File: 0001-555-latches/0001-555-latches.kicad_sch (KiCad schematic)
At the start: 27 parts, among them J1 DC_IN, J2 ASTBL_OUT, J3 MSTBL_OUT, J4 BSTBL_OUT, SW1 SW_Push, SW2 SW_Push, SW3 SW_Push, U1 NE555P, U2 NE555P, U3 NE555P

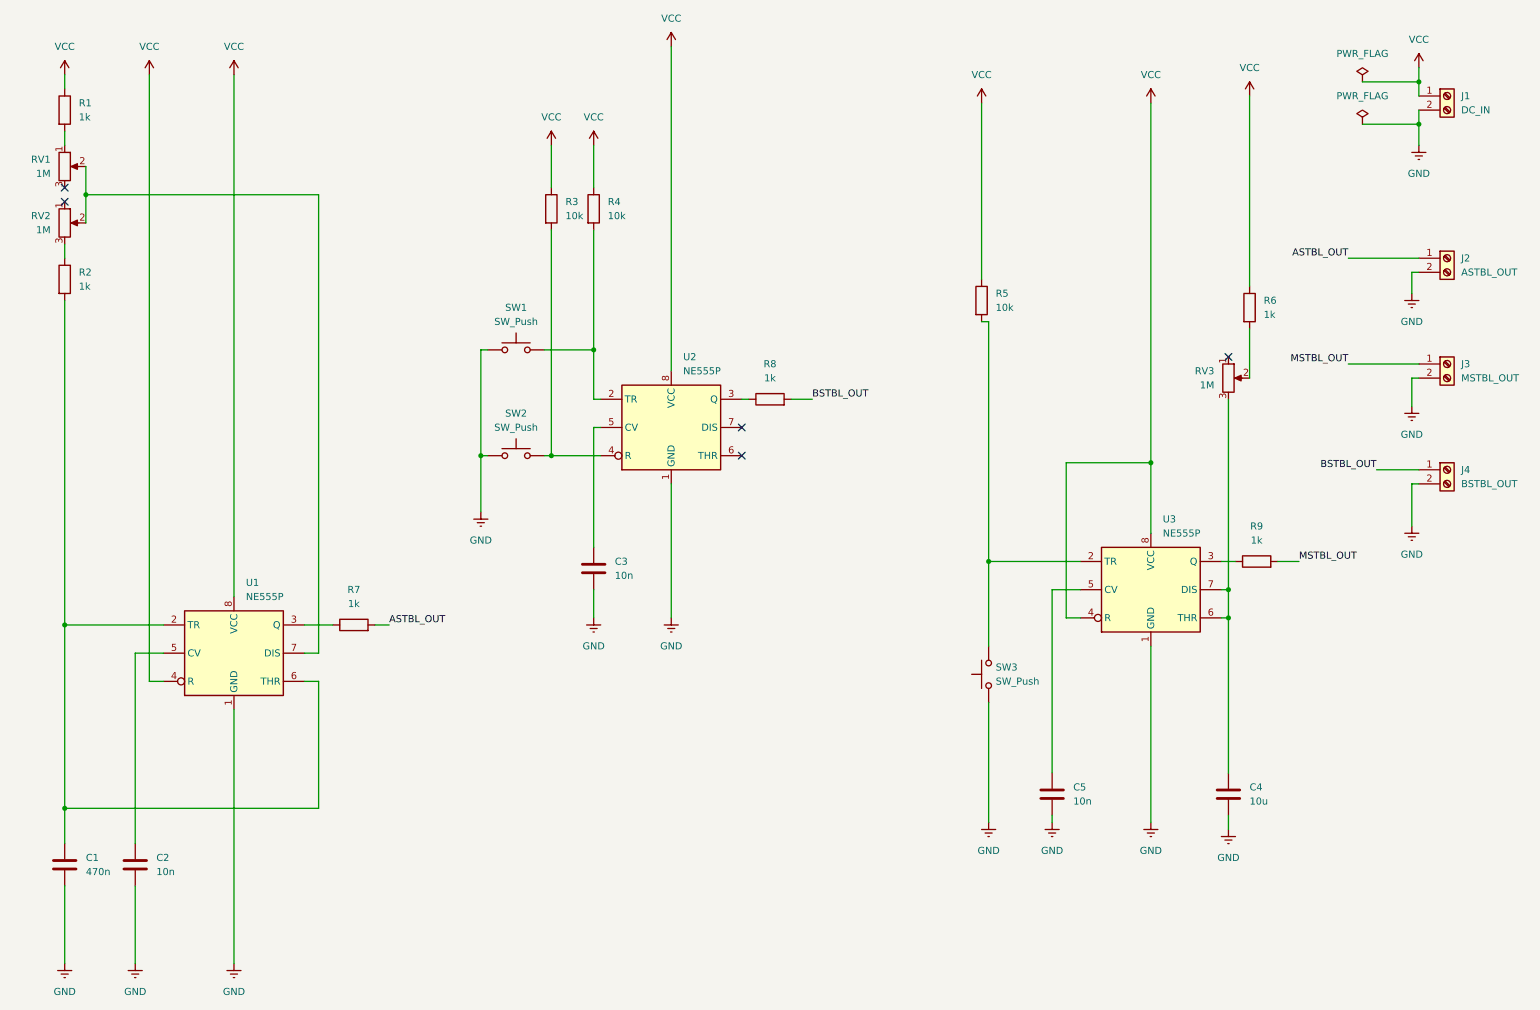
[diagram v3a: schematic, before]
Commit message: Update values and symbols of monostable capacitor
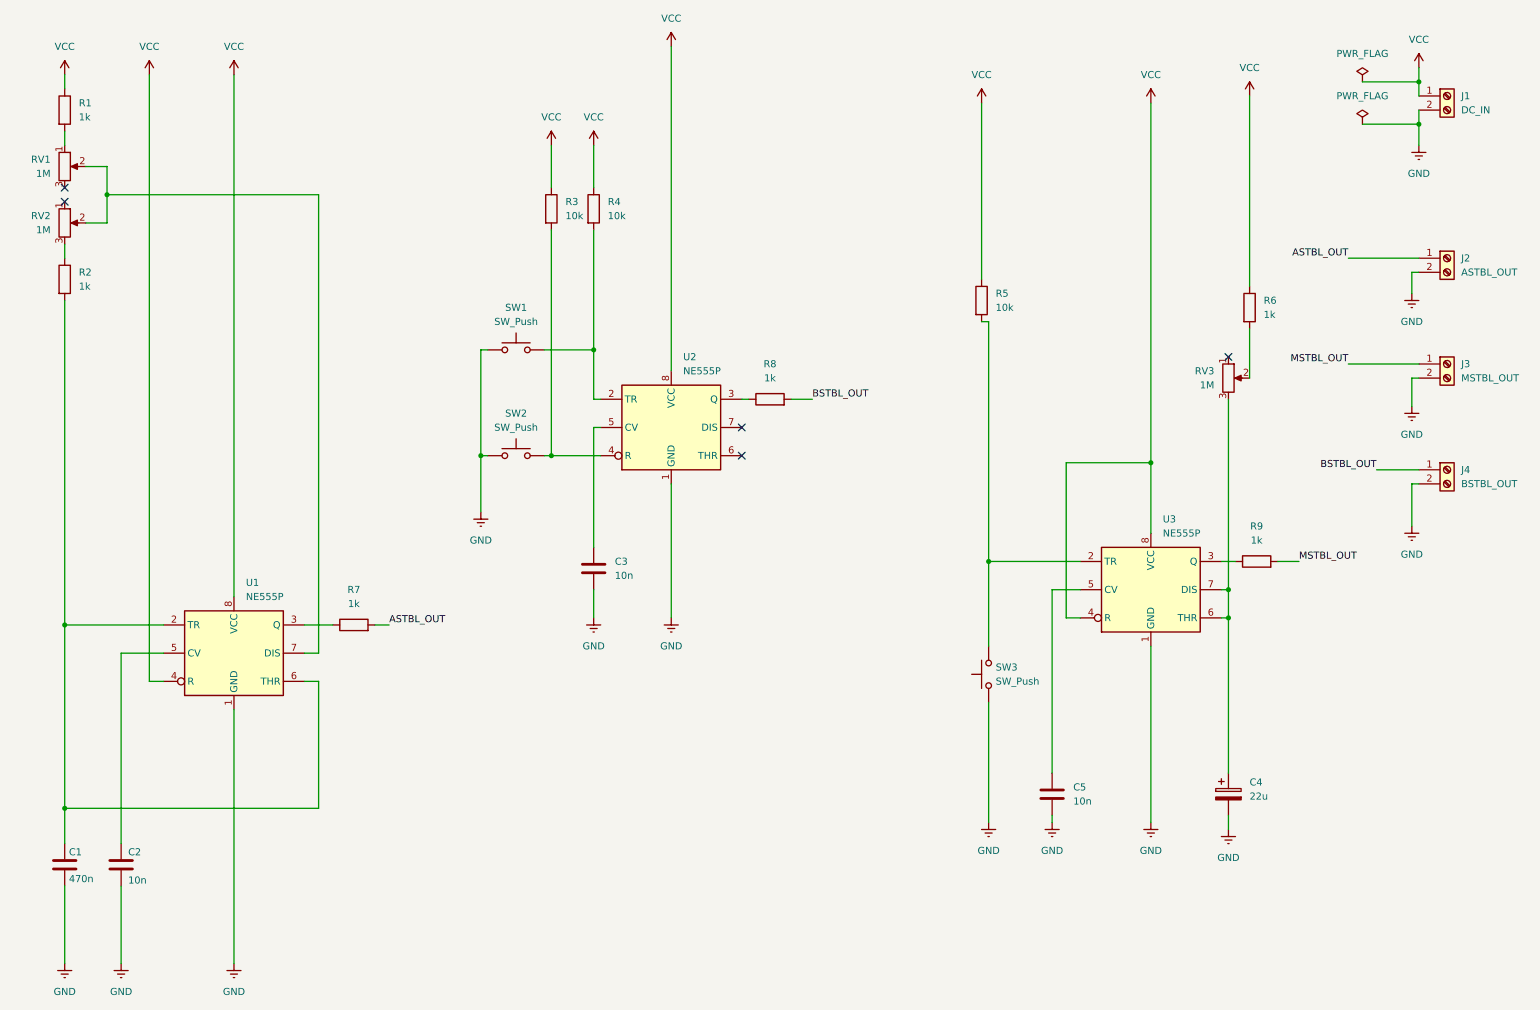
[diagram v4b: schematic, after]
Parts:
- removed C4: 10u, symbol Device:C
- added C4: 22u, symbol Device:C_Polarized
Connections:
- net GND: now also C4.2
- net at RV3.3, U3.6 (THR), U3.7 (DIS): now also C4.1
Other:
- moved on the sheet: C2
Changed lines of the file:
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@@
 	)
 	(junction
-		(at 24.13 46.99)
+		(at 27.94 46.99)
 		(diameter 0)
 		(color 0 0 0 0)
@@
 	(wire
 		(pts
-			(xy 24.13 41.91) (xy 24.13 46.99)
+			(xy 27.94 41.91) (xy 27.94 46.99)
 		)
 		(stroke
@@
 	(wire
 		(pts
-			(xy 33.02 163.83) (xy 33.02 129.54)
+			(xy 30.48 163.83) (xy 30.48 129.54)
 		)
 		(stroke
@@
 	(wire
 		(pts
-			(xy 33.02 171.45) (xy 33.02 185.42)
+			(xy 30.48 171.45) (xy 30.48 185.42)
 		)
 		(stroke
@@
 	(wire
 		(pts
+			(xy 27.94 52.07) (xy 24.13 52.07)
+		)
+		(stroke
+			(width 0)
+			(type default)
+		)
+	)
+	(wire
+		(pts
 			(xy 264.16 38.1) (xy 264.16 34.29)
 		)
@@
 	(wire
 		(pts
-			(xy 24.13 46.99) (xy 66.04 46.99)
+			(xy 27.94 46.99) (xy 66.04 46.99)
 		)
 		(stroke
@@
 	(wire
 		(pts
-			(xy 24.13 46.99) (xy 24.13 52.07)
+			(xy 27.94 46.99) (xy 27.94 52.07)
 		)
 		(stroke
@@
 	(wire
 		(pts
+			(xy 27.94 41.91) (xy 24.13 41.91)
+		)
+		(stroke
+			(width 0)
+			(type default)
+		)
+	)
+	(wire
+		(pts
 			(xy 66.04 134.62) (xy 63.5 134.62)
 		)
@@
 	(wire
 		(pts
-			(xy 33.02 129.54) (xy 38.1 129.54)
+			(xy 30.48 129.54) (xy 38.1 129.54)
 		)
 		(stroke
@@
 	(symbol
 		(lib_id "power:GNDREF")
-		(at 33.02 185.42 0)
+		(at 30.48 185.42 0)
 		(unit 1)
 		(exclude_from_sim no)
@@
 		(fields_autoplaced yes)
 		(property "Reference" "#PWR03"
-			(at 33.02 191.77 0)
+			(at 30.48 191.77 0)
 			(effects
 				(font
@@
 		)
 		(property "Value" "GND"
-			(at 33.02 190.5 0)
+			(at 30.48 190.5 0)
 			(effects
 				(font
@@
 		)
 		(property "Footprint" ""
-			(at 33.02 185.42 0)
+			(at 30.48 185.42 0)
 			(effects
 				(font
@@
 		)
 		(property "Datasheet" ""
-			(at 33.02 185.42 0)
+			(at 30.48 185.42 0)
 			(effects
 				(font
@@
 		)
 		(property "Description" "Power symbol creates a global label with name \"GNDREF\" , reference supply ground"
-			(at 33.02 185.42 0)
+			(at 30.48 185.42 0)
 			(effects
 				(font
@@
 	(symbol
 		(lib_id "Device:C")
-		(at 33.02 167.64 0)
+		(at 30.48 167.64 0)
 		(unit 1)
 		(exclude_from_sim no)
@@
 		(on_board yes)
 		(dnp no)
-		(fields_autoplaced yes)
 		(property "Reference" "C2"
-			(at 36.83 166.3699 0)
+			(at 31.75 165.354 0)
 			(effects
 				(font
@@
 		)
 		(property "Value" "10n"
-			(at 36.83 168.9099 0)
+			(at 31.75 170.434 0)
 			(effects
 				(font
@@
 		)
 		(property "Footprint" ""
-			(at 33.9852 171.45 0)
+			(at 31.4452 171.45 0)
 			(effects
 				(font
@@
 		)
 		(property "Datasheet" "~"
-			(at 33.02 167.64 0)
+			(at 30.48 167.64 0)
 			(effects
 				(font
@@
 		)
 		(property "Description" "Unpolarized capacitor"
-			(at 33.02 167.64 0)
+			(at 30.48 167.64 0)
 			(effects
 				(font
@@
 		(on_board yes)
 		(dnp no)
-		(fields_autoplaced yes)
 		(property "Reference" "C1"
-			(at 24.13 166.3699 0)
+			(at 21.082 165.354 0)
 			(effects
 				(font
@@
 		)
 		(property "Value" "470n"
-			(at 24.13 168.9099 0)
+			(at 21.082 170.18 0)
 			(effects
 				(font
@@
 	)
 	(symbol
+		(lib_id "Device:C_Polarized")
+		(at 229.87 154.94 0)
+		(unit 1)
+		(exclude_from_sim no)
+		(in_bom yes)
+		(on_board yes)
+		(dnp no)
+		(fields_autoplaced yes)
+		(property "Reference" "C4"
+			(at 233.68 152.7809 0)
+			(effects
+				(font
+					(size 1.27 1.27)
+				)
+				(justify left)
+			)
+		)
+		(property "Value" "22u"
+			(at 233.68 155.3209 0)
+			(effects
+				(font
+					(size 1.27 1.27)
+				)
+				(justify left)
+			)
+		)
+		(property "Footprint" ""
+			(at 230.8352 158.75 0)
+			(effects
+				(font
+					(size 1.27 1.27)
+				)
+				(hide yes)
+			)
+		)
+		(property "Datasheet" "~"
+			(at 229.87 154.94 0)
+			(effects
+				(font
+					(size 1.27 1.27)
+				)
+				(hide yes)
+			)
+		)
+		(property "Description" "Polarized capacitor"
+			(at 229.87 154.94 0)
+			(effects
+				(font
+					(size 1.27 1.27)
+				)
+				(hide yes)
+			)
+		)
+		(pin "1"
+		)
+		(pin "2"
+		)
+		(instances
+			(project ""
+				(path "/11cec59d-a989-4950-8b21-3f1fb45ca1cc"
+					(reference "C4")
+					(unit 1)
+				)
+			)
+		)
+	)
+	(symbol
 		(lib_id "Connector:Screw_Terminal_01x02")
 		(at 269.24 29.21 0)
@@
 					(unit 1)
 				)
-			)
-		)
-	)
-	(symbol
-		(lib_id "Device:C")
-		(at 229.87 154.94 0)
-		(unit 1)
-		(exclude_from_sim no)
-		(in_bom yes)
-		(on_board yes)
-		(dnp no)
-		(fields_autoplaced yes)
-		(property "Reference" "C4"
-			(at 233.68 153.6699 0)
-			(effects
-				(font
-					(size 1.27 1.27)
-				)
-				(justify left)
-			)
-		)
-		(property "Value" "10u"
-			(at 233.68 156.2099 0)
-			(effects
-				(font
-					(size 1.27 1.27)
-				)
-				(justify left)
-			)
-		)
-		(property "Footprint" ""
-			(at 230.8352 158.75 0)
-			(effects
-				(font
-					(size 1.27 1.27)
-				)
-				(hide yes)
-			)
-		)
-		(property "Datasheet" "~"
-			(at 229.87 154.94 0)
-			(effects
-				(font
-					(size 1.27 1.27)
-				)
-				(hide yes)
-			)
-		)
-		(property "Description" "Unpolarized capacitor"
-			(at 229.87 154.94 0)
-			(effects
-				(font
-					(size 1.27 1.27)
-				)
-				(hide yes)
-			)
-		)
-		(pin "1"
-		)
-		(pin "2"
-		)
-		(instances
-			(project ""
-				(path "/11cec59d-a989-4950-8b21-3f1fb45ca1cc"
-					(reference "C4")
-					(unit 1)
-				)

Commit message: Improve schematics layout
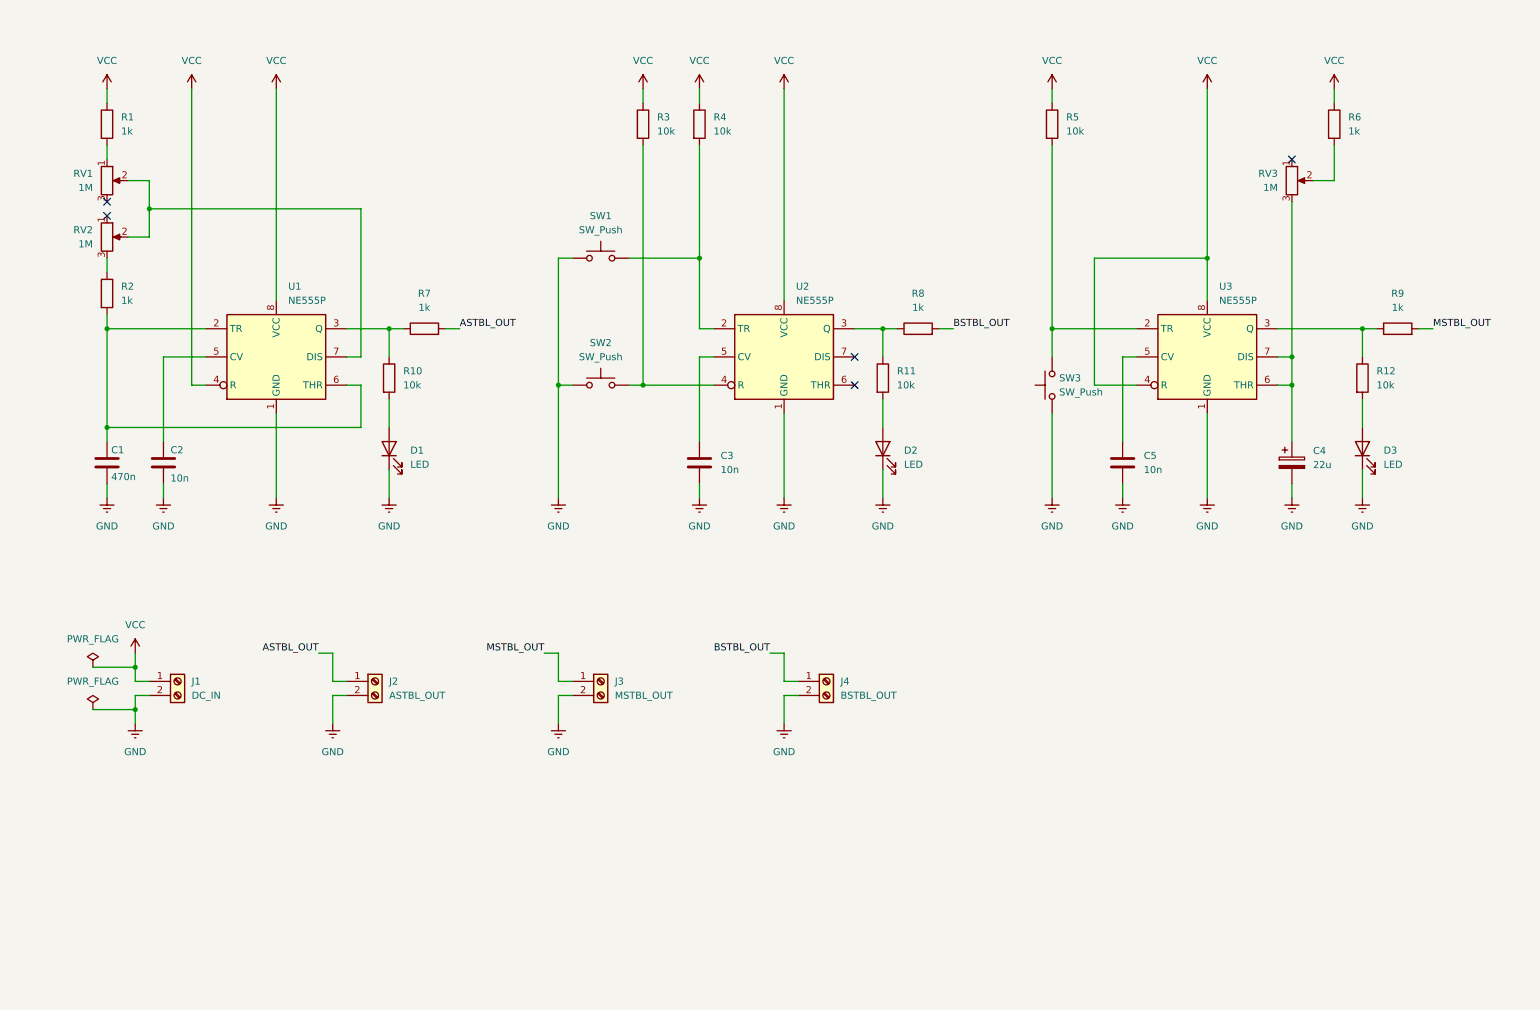
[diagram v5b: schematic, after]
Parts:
- added D1, D2, D3: LED, symbol Device:LED
- added R10, R11, R12: 10k, symbol Device:R
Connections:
- net GND: now also D1.1 (K), D2.1 (K), D3.1 (K)
- net at R7.1, U1.3 (Q): now also R10.1
- net at R8.1, U2.3 (Q): now also R11.1
- net at R9.1, U3.3 (Q): now also R12.1
- new net: D1.2 (A), R10.2
- new net: D3.2 (A), R12.2
- new net: D2.2 (A), R11.2
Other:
- moved on the sheet: C1, C2, C3, C4, C5, J1, J2, J3, J4, R1, R2, R3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

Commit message: Update version
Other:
- company: (none) -> https://github.com/marcinciapa-el/0001
- title: 0001: 555 Latches -> 555 Latches
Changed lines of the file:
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@@
 	(paper "A4")
 	(title_block
-		(title "0001: 555 Latches")
-		(date "2025-10-06")
-		(rev "01")
+		(title "555 Latches")
+		(date "2025-10-08")
+		(rev "v0.0.1")
+		(company "https://github.com/marcinciapa-el/0001")
 	)
 	(junction

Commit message: Fixes after tutorials
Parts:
- C1: value 470n -> 470nF
- C2, C3, C5: value 10n -> 10nF
- C4: value 22u -> 22uF
- D1: value LED -> RED
- D2: value LED -> GREEN
- D3: value LED -> YELLO
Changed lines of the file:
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@@
 			)
 		)
-		(property "Value" "LED"
+		(property "Value" "RED"
 			(at 82.55 95.5674 90)
 			(effects
@@
 			)
 		)
-		(property "Value" "10n"
+		(property "Value" "10nF"
 			(at 138.43 96.5199 0)
 			(effects
@@
 			)
 		)
-		(property "Value" "10n"
+		(property "Value" "10nF"
 			(at 214.63 96.5199 0)
 			(effects
@@
 			)
 		)
-		(property "Value" "10n"
+		(property "Value" "10nF"
 			(at 39.37 98.044 0)
 			(effects
@@
 			)
 		)
-		(property "Value" "470n"
+		(property "Value" "470nF"
 			(at 28.702 97.79 0)
 			(effects
@@
 			)
 		)
-		(property "Value" "22u"
+		(property "Value" "22uF"
 			(at 245.11 95.6309 0)
 			(effects
@@
 			)
 		)
-		(property "Value" "LED"
+		(property "Value" "YELLO"
 			(at 257.81 95.5674 90)
 			(effects
@@
 			)
 		)
-		(property "Value" "LED"
+		(property "Value" "GREEN"
 			(at 171.45 95.5674 90)
 			(effects
